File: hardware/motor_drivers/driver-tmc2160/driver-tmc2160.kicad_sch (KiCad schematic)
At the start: 57 parts, among them M1 Micro-Fit 3.0, Q1 30N06, Q2 30N06, Q3 30N06, Q4 30N06, Q5 30N06, Q6 30N06, Q7 30N06, Q8 30N06, T1 GND, T10 SCK, T11 GND, T12 DIR, T13 ENCB, T14 SDI, T15 EN, T16 ENCN, T17 SDO, T18 VCC, T19 SPI_MODE, T2 CS0, T20 SD_MODE, T21 Therm, T3 DIAG0, T4 CLK, T5 STEP, T6 DIAG1, T7 12V, T8 GND, T9 ENCA, U1 TMC2160

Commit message: aonteuhasntoidanouidoenuthidntoehuid
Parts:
- added C12: 4.7nF, AlphaLib:0402C, symbol Device:C_Small
- added C13: 10nF, AlphaLib:0402C, symbol Device:C_Small
- added D2: Y, AlphaLib:0603LED, symbol Device:LED_Small
- added D3: R, AlphaLib:0603LED, symbol Device:LED_Small
- added R14: DkΩ, AlphaLib:0402R, symbol Device:R_Small
- added R15: EkΩ, AlphaLib:0402R, symbol Device:R_Small
- added R16: 1kΩ, AlphaLib:0402R, symbol Device:R_Small
- added R17: 200Ω, AlphaLib:0402R, symbol Device:R_Small
- added R5: AkΩ, AlphaLib:0402R, symbol Device:R_Small
- added R6: BkΩ, AlphaLib:0402R, symbol Device:R_Small
- added R7: CkΩ, AlphaLib:0402R, symbol Device:R_Small
- added U2: LM393, Package_SO:MSOP-8_3x3mm_P0.65mm, symbol corevus:LM393
- D1: value Red -> G
- TH1: value 10kΩ 3380K -> 10kΩ 3950K
- renumbered T2 to T10, T5 to T11, T8 to T12, T12 to T13, T15 to T14, T19 to T15, T20 to T16, T3 to T17, T6 to T18, T9 to T19, T4 to T2, T13 to T20, T16 to T21, T7 to T3, T10 to T4, T11 to T5, T14 to T6, T17 to T7, T18 to T8, T21 to T9
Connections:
- net _{M0}Dir is gone; now on net Dir: U1.18 (DIR)
- net _{M0}Stall is gone; now on net Diag0: U1.26 (DIAG0)
- net _{M0}Step is gone; now on net Step: U1.17 (STEP)
- net _{M0}~{En} is gone; now on net ~{En}: R1.2, R2.2, U1.28 (~{DRV_EN})
- net Diag1: now also U1.27 (DIAG1), R16.2
- net GND: now also C12.2, C13.2, R6.2, U2.4 (V-)
- net THERM: now also C13.1, U2.5 (+)
- net VCC: now also D2.2 (A), R14.1, R17.1, R5.2, U2.8 (V+)
- new net: D3.2 (A), R17.2
- new net: D2.1 (K), R16.1
- new net: C12.1, R15.2, U2.2 (-), U2.6 (-)
- new net: R14.2, R15.1, R7.2, U2.1
- new net: R5.1, R6.1, R7.1, U2.3 (+)
- new net: D3.1 (K), U2.7
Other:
- moved on the sheet: H1, H2, M1, Q1, Q2, Q3, Q4, Q5, Q6, Q7, Q8, R10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

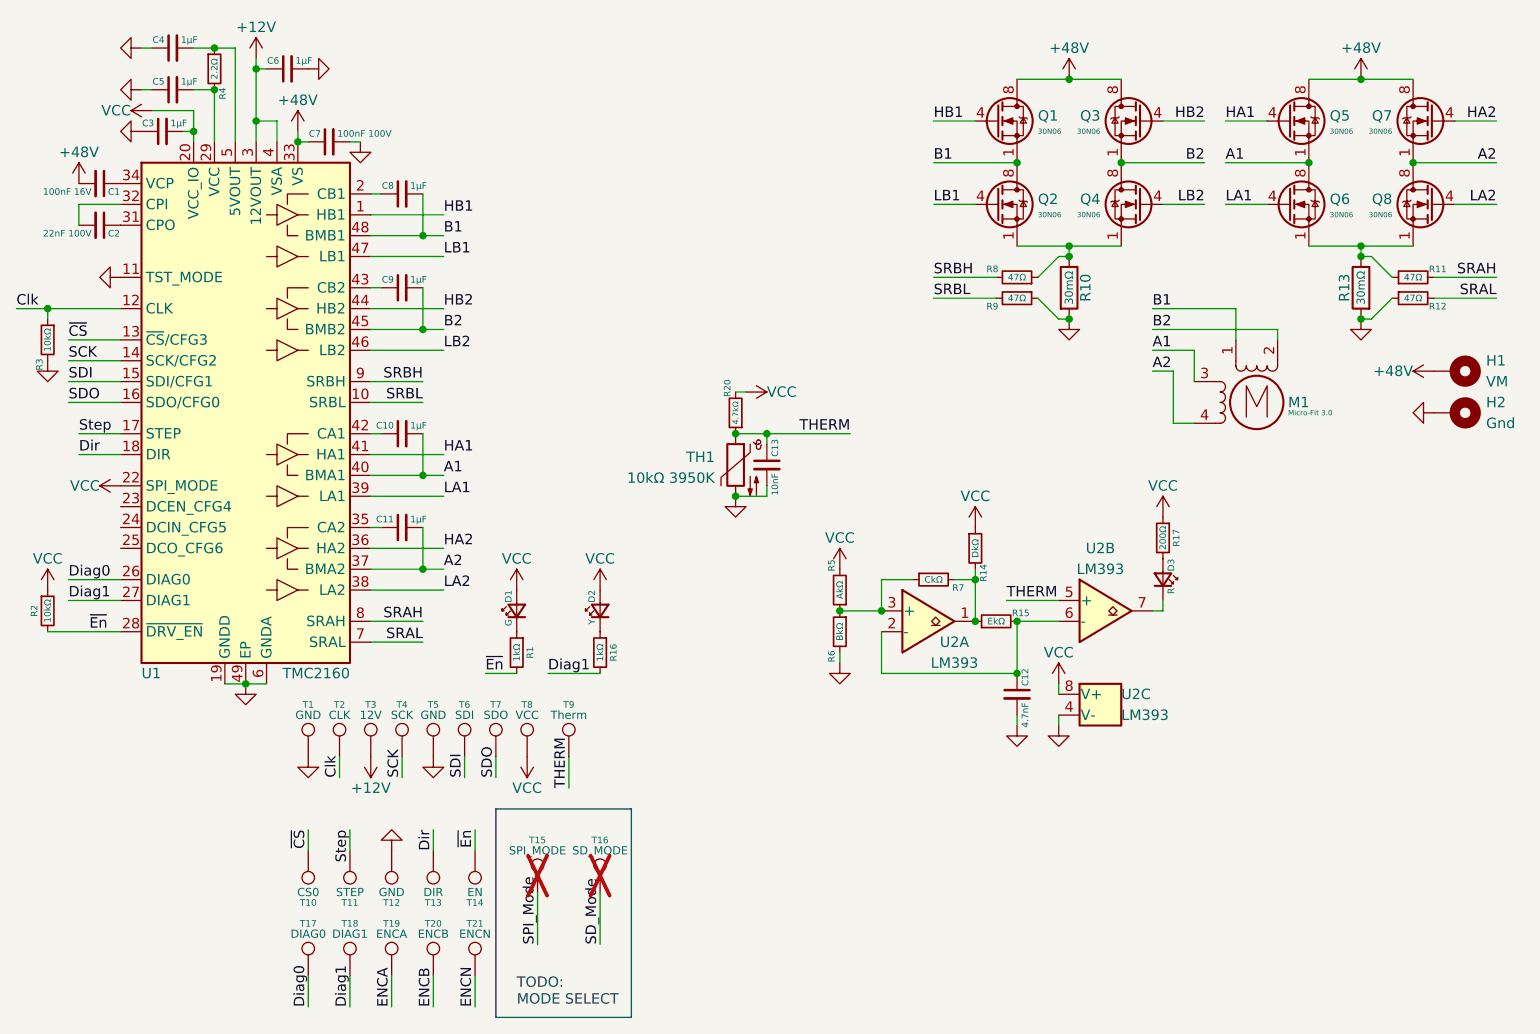
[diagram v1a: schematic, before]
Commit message: v0.4 mostly complete, board needs minor revisions (e.g. pin swap)
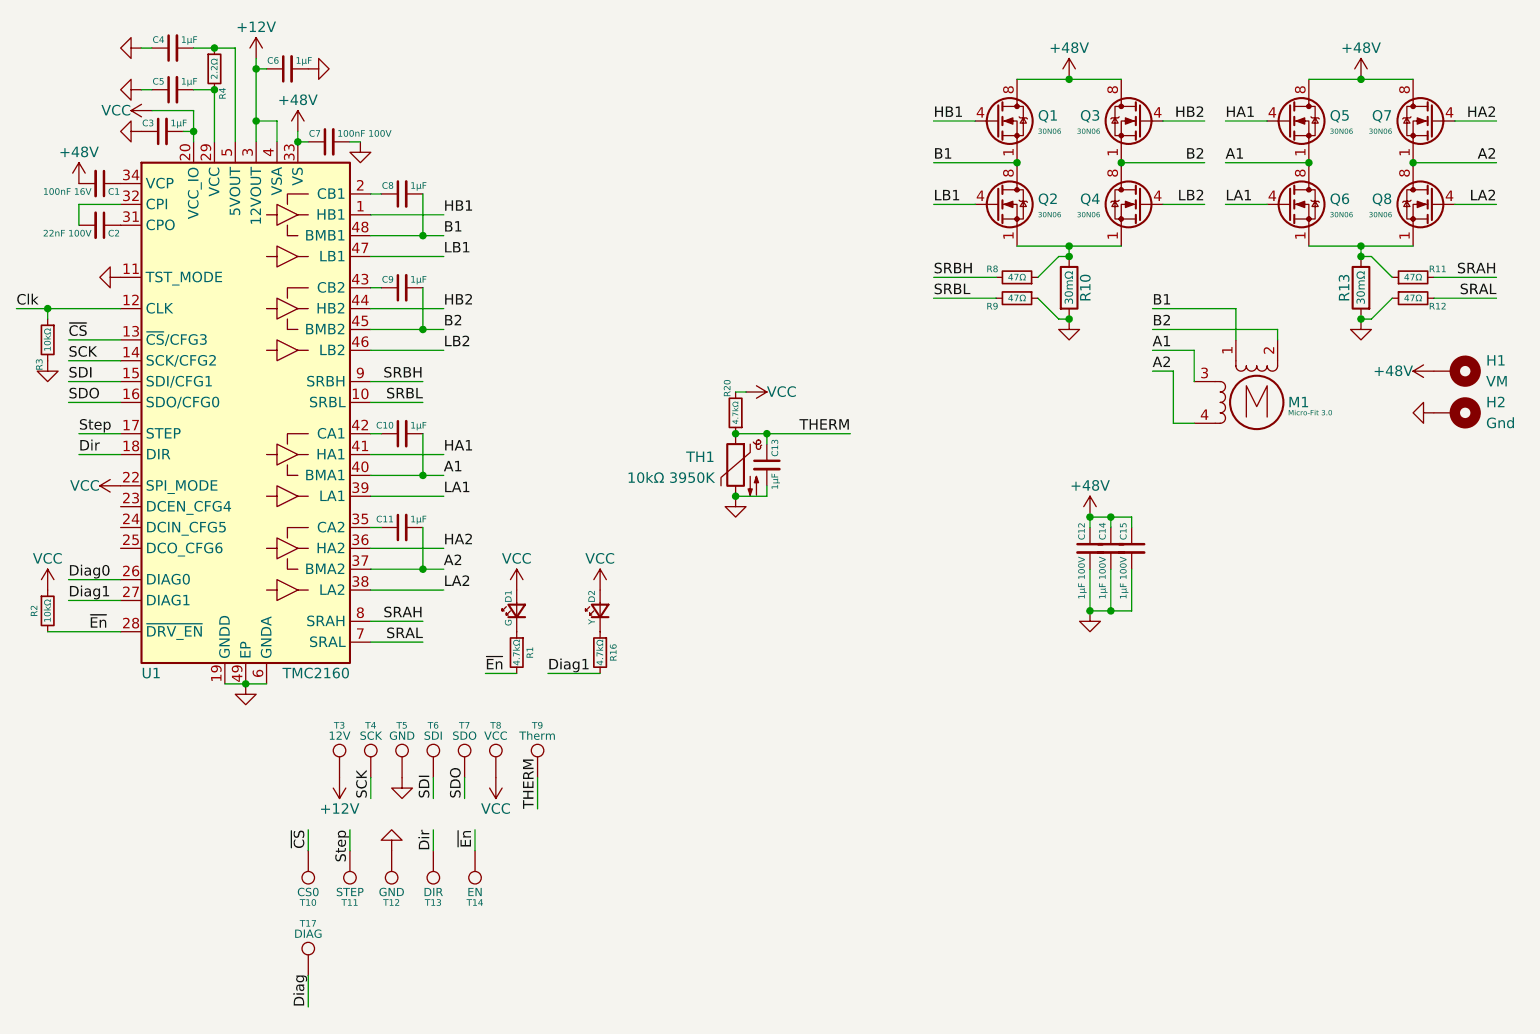
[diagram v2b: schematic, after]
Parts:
- removed D3: R, AlphaLib:0603LED, symbol Device:LED_Small
- removed R14: DkΩ, AlphaLib:0402R, symbol Device:R_Small
- removed R15: EkΩ, AlphaLib:0402R, symbol Device:R_Small
- removed R17: 200Ω, AlphaLib:0402R, symbol Device:R_Small
- removed R5: AkΩ, AlphaLib:0402R, symbol Device:R_Small
- removed R6: BkΩ, AlphaLib:0402R, symbol Device:R_Small
- removed R7: CkΩ, AlphaLib:0402R, symbol Device:R_Small
- removed T1: GND, corevus:LGA_Land, symbol Connector:TestPoint
- removed T15: SPI_MODE, corevus:LGA_Land, symbol Connector:TestPoint
- removed T16: SD_MODE, corevus:LGA_Land, symbol Connector:TestPoint
- removed T18: DIAG1, corevus:LGA_Land, symbol Connector:TestPoint
- removed T19: ENCA, corevus:LGA_Land, symbol Connector:TestPoint
- removed T2: CLK, corevus:LGA_Land, symbol Connector:TestPoint
- removed T20: ENCB, corevus:LGA_Land, symbol Connector:TestPoint
- removed T21: ENCN, corevus:LGA_Land, symbol Connector:TestPoint
- removed U2: LM393, Package_SO:MSOP-8_3x3mm_P0.65mm, symbol corevus:LM393
- added C14, C15: 1μF 100V, Capacitor_SMD:C_1206_3216Metric, symbol Device:C_Small
- C12: value 4.7nF -> 1μF 100V; footprint AlphaLib:0402C -> Capacitor_SMD:C_1206_3216Metric
- C13: value 10nF -> 1μF
- R1, R16: value 1kΩ -> 4.7kΩ
- T10, T11, T12, T13, T14, T3, T4, T5, T6, T7, T8, T9: footprint corevus:LGA_Land -> corevus:LGA_Land_2.5mm
- T17: value DIAG0 -> DIAG; footprint corevus:LGA_Land -> corevus:LGA_Land_2.5mm
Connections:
- net +48V: now also C12.1, C14.1, C15.1
- net Diag0: no longer T17.1
- net GND: now also C14.2, C15.2
- new net Diag: T17.1
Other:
- note removed: "TODO: MODE SELECT"
- moved on the sheet: T3, T4, T5, T6, T7, T8, T9

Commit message: CvG v0.4 complete, now updating documentation
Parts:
- added H3, H4: MountingHole, corevus:ToolingHole, symbol Mechanical:MountingHole
- added TP1, TP2, TP3, TP4: TestPoint, TestPoint:TestPoint_Pad_D1.0mm, symbol Connector:TestPoint
- M1: value Micro-Fit 3.0 -> JST XH; footprint corevus:XKB_X3025WRS-04D -> corevus:XKB_X8821WRS-04
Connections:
- net Diag is gone; now on net Diag1: T17.1
- net A1: now also M1.2 (-); no longer M1.3
- net A2: now also M1.1; no longer M1.4
- net B1: now also M1.4; no longer M1.1
- net B2: now also M1.3; no longer M1.2 (-)
- net GND: now also TP2.1
- net LB1: now also TP3.1
- net SRBH: now also TP4.1
- net VCC: now also TP1.1

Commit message: should be up to date for cvg v0.6 and latest protected drivers
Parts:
- added C16, C17, C18, C19: 1nF 100V, PCM_ME_passives:0402C, symbol Device:C_Small
- added C20, C21: 1nF, PCM_ME_passives:0402C, symbol Device:C_Small
- added D3, D4: BAV99S, Package_TO_SOT_SMD:SOT-363_SC-70-6, symbol Diode:BAV99S
- added FB1, FB2, FB3, FB4: 30Ω@100MHz, Resistor_SMD:R_0805_2012Metric, symbol Device:FerriteBead_Small
- C1: value 100nF 16V -> 1μF 25V
- C10, C11, C8, C9: value 1μF -> 1μF 25V
- C2: value 22nF 100V -> 100nF 100V
- D1: value G -> Red; footprint AlphaLib:0603LED -> PCM_ME_passives:0402LED
- D2: value Y -> Green; footprint AlphaLib:0603LED -> PCM_ME_passives:0402LED
- H1, H2: now left out of the parts list
- H3: value MountingHole -> ToolingHole; now left out of the parts list
- H4: value MountingHole -> ToolingHole; now not fitted; now left out of the parts list
- J1: renamed from M1; value JST XH -> XH; footprint corevus:XKB_X8821WRS-04 -> corevus:XH_1x04_SMD_Vertical; symbol Motor:Stepper_Motor_bipolar -> Connector_Generic:Conn_01x04
- R10, R13: value 30mΩ -> 50mΩ
- R16: value 4.7kΩ -> 1kΩ
- R4: value 2.2Ω -> 1Ω
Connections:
- net +48V: now also D3.2 (K2), D3.5 (K4), D4.2 (K2), D4.5 (K4)
- net A1: now also FB2.2; no longer J1.2 (-)
- net A2: now also FB1.2; no longer J1.1
- net B1: now also FB4.2; no longer J1.4
- net B2: now also FB3.2; no longer J1.3
- net GND: now also C16.1, C17.1, C18.1, C19.1, D3.1 (A1), D3.4 (A3), D4.1 (A1), D4.4 (A3)
- net SRAH: now also C21.2
- net SRAL: now also C21.1
- net SRBH: now also C20.2
- net SRBL: now also C20.1
- new net A1': C17.2, D4.6 (K3A4), FB2.1, J1.2 (Pin_2)
- new net A2': C16.2, D4.3 (K1A2), FB1.1, J1.1 (Pin_1)
- new net B1': C19.2, D3.3 (K1A2), FB4.1, J1.4 (Pin_4)
- new net B2': C18.2, D3.6 (K3A4), FB3.1, J1.3 (Pin_3)
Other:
- company: (none) -> meridi engineering
- title: (none) -> TMC2160 Stepper Driver Module
- moved on the sheet: C12, C14, C15, D2, H1, H2, H3, R10, R11, R12, R13, R8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
